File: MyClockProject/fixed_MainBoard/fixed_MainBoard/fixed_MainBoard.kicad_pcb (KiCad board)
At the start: 2 copper layers, 106.7 x 69.8 mm, 20 parts, among them J1 USB_C_Receptacle_PowerOnly_6P, J2 RJ45, J5 Conn_01x05_Socket, J6 Conn_01x16_Socket, J7 Conn_01x08_Socket, J8 Conn_01x03_Socket, J9 Barrel_Jack, U1 ULN2003A

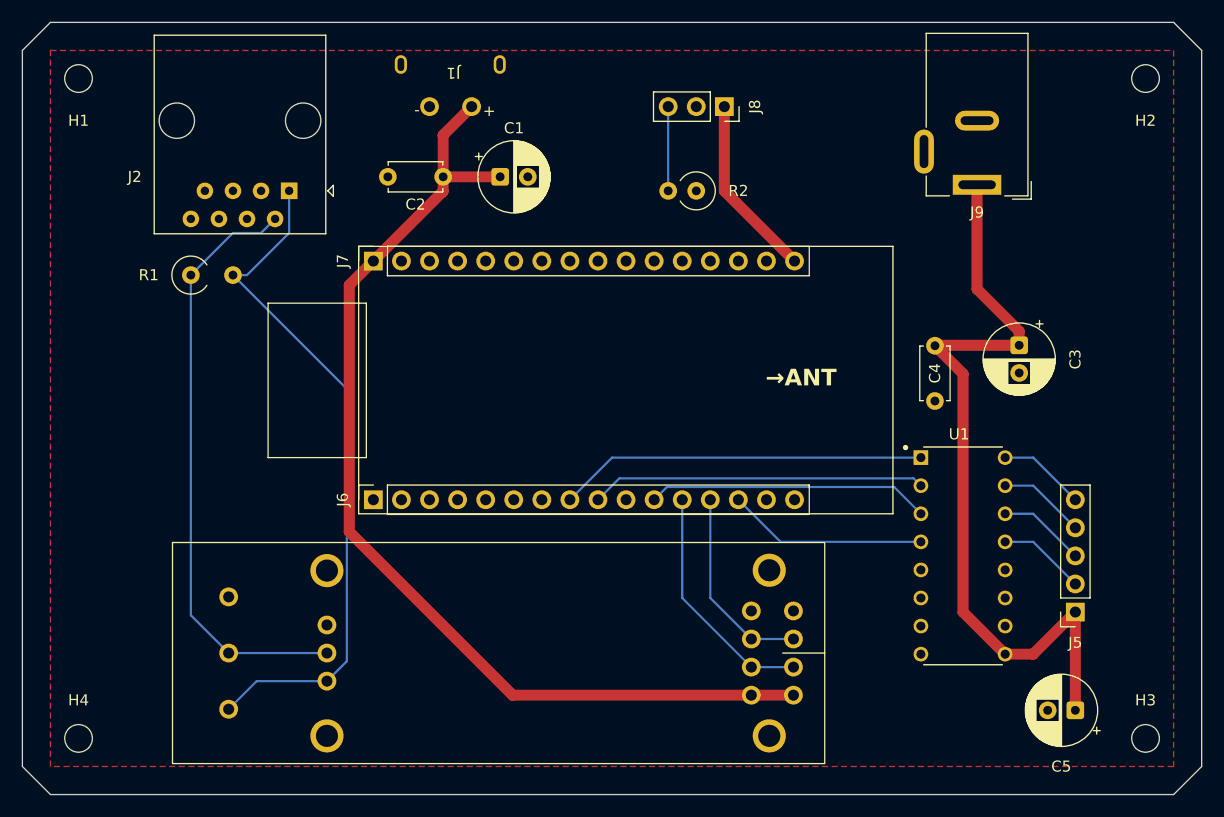
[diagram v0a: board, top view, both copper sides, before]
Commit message: SwitchBoxとMainboardのTTLコンバーターの穴位置を修正。余計なファイルを削除
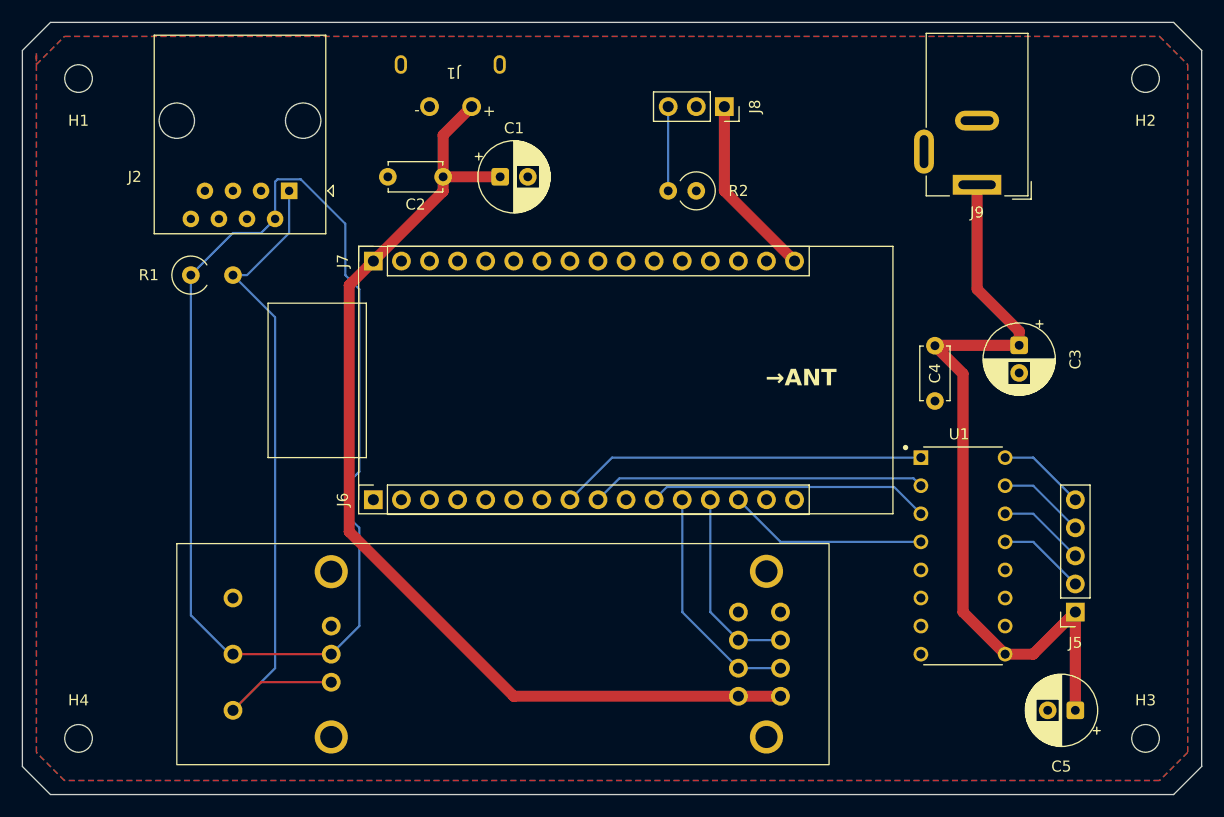
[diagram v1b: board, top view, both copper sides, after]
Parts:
- moved ? 45.7 mm to (135.9, 120.7)
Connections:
- J6 pad 15: Net-(J6-Pin_15) -> (no net)
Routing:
- net Net-(J2-Pin_2): track 54.2 -> 107.3 mm
- net Net-(J1_5V): track 94.5 -> 93.4 mm
- net Net-(J2-Pin_1): track 62.2 -> 62.9 mm
- added copper zone on B.Cu, net GND
